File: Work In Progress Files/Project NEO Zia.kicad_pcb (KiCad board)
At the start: 2 copper layers, 220.2 x 220.2 mm, 149 parts, among them J1 TSM-103-02-L-SH-LC, J2 TSM-103-02-L-SH-LC, J3 Conn_01x02, U2 LM1084IS-5.0_NOPB

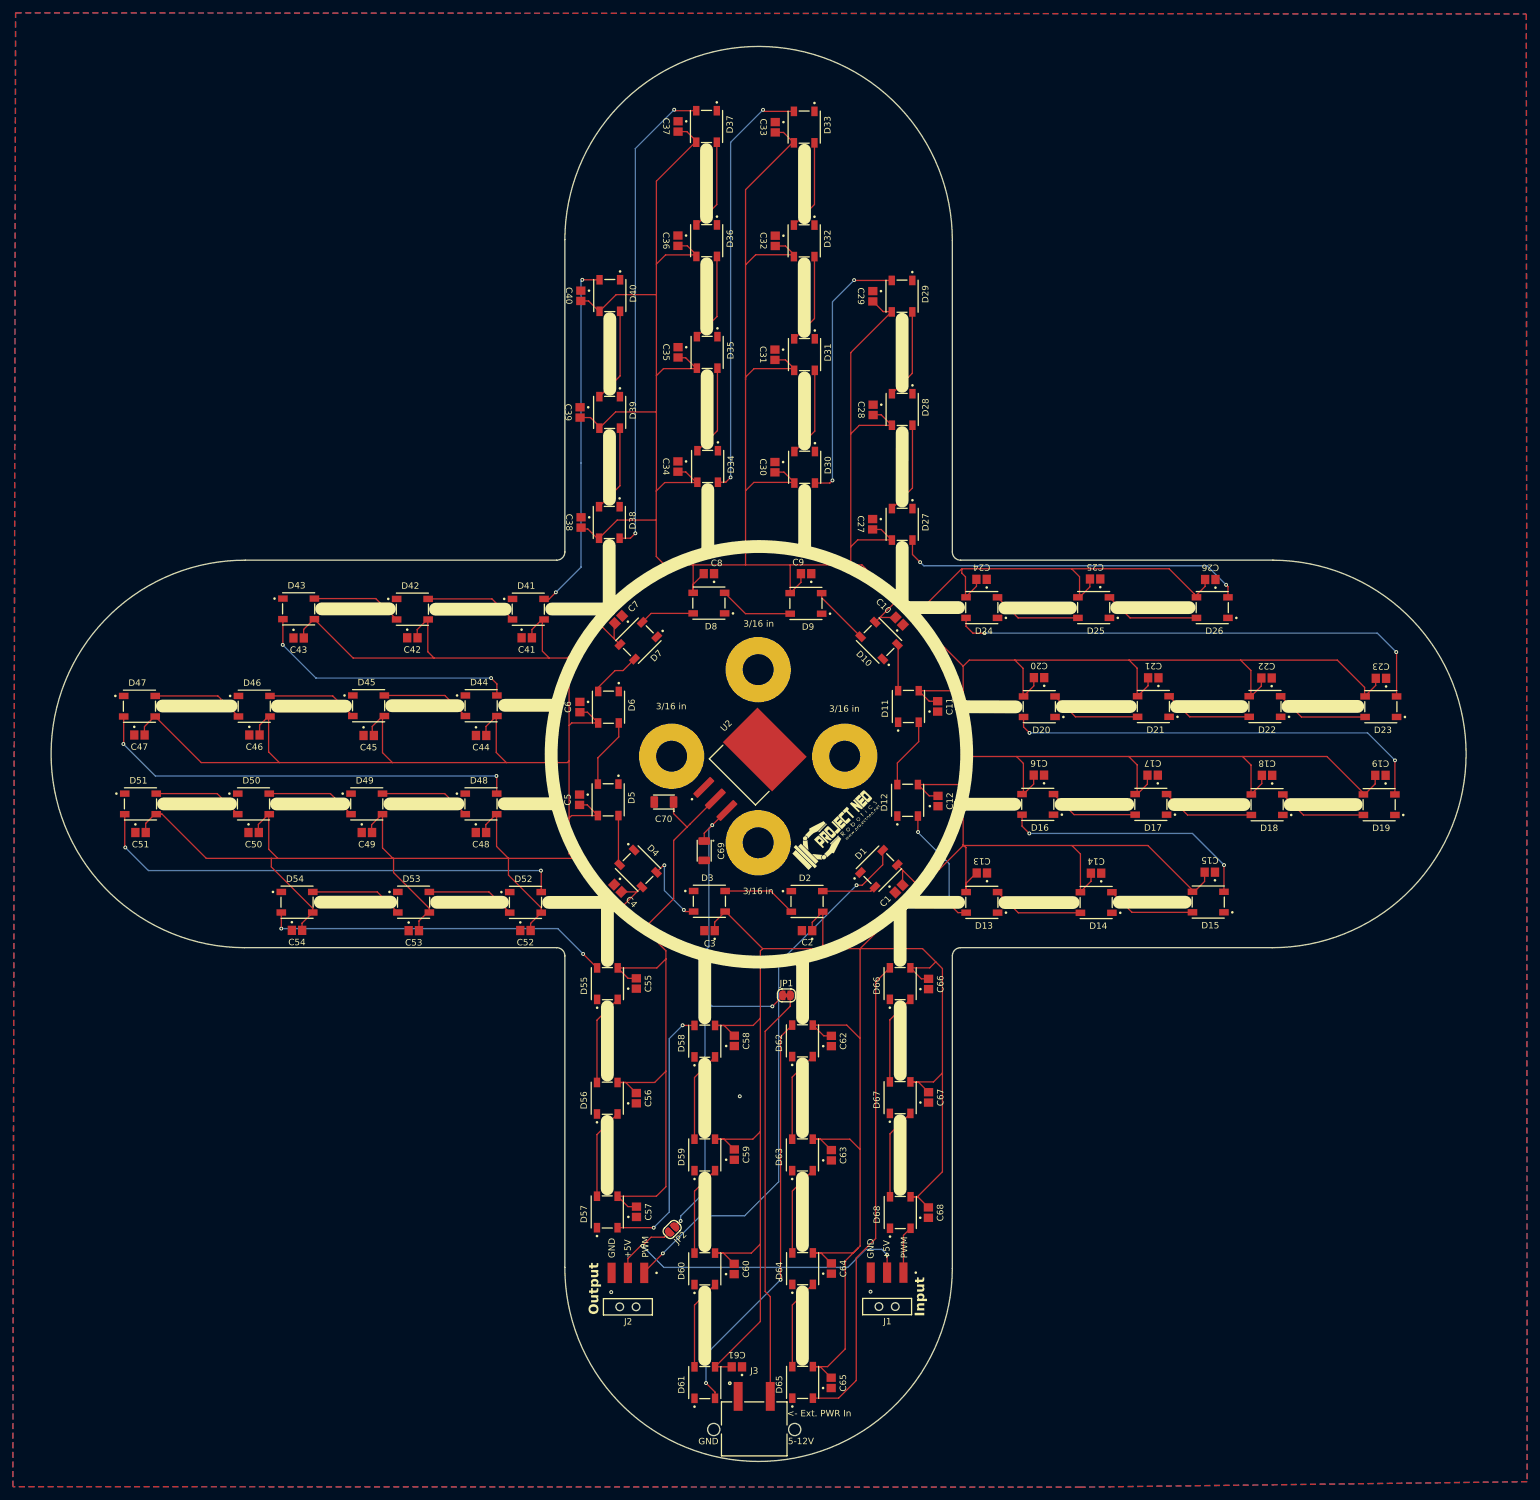
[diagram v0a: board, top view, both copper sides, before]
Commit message: - Added 5V copper plane in center for TI LM1084 voltage regulator - Rearranged filter capacitors for voltage regulator and some NeoPixel's - Added REV marker to board 	# On Rear Silkscreen - Added Jumper Config. Table 	# On Rear Silkscreen - Moved Designer name to rear silkscreen
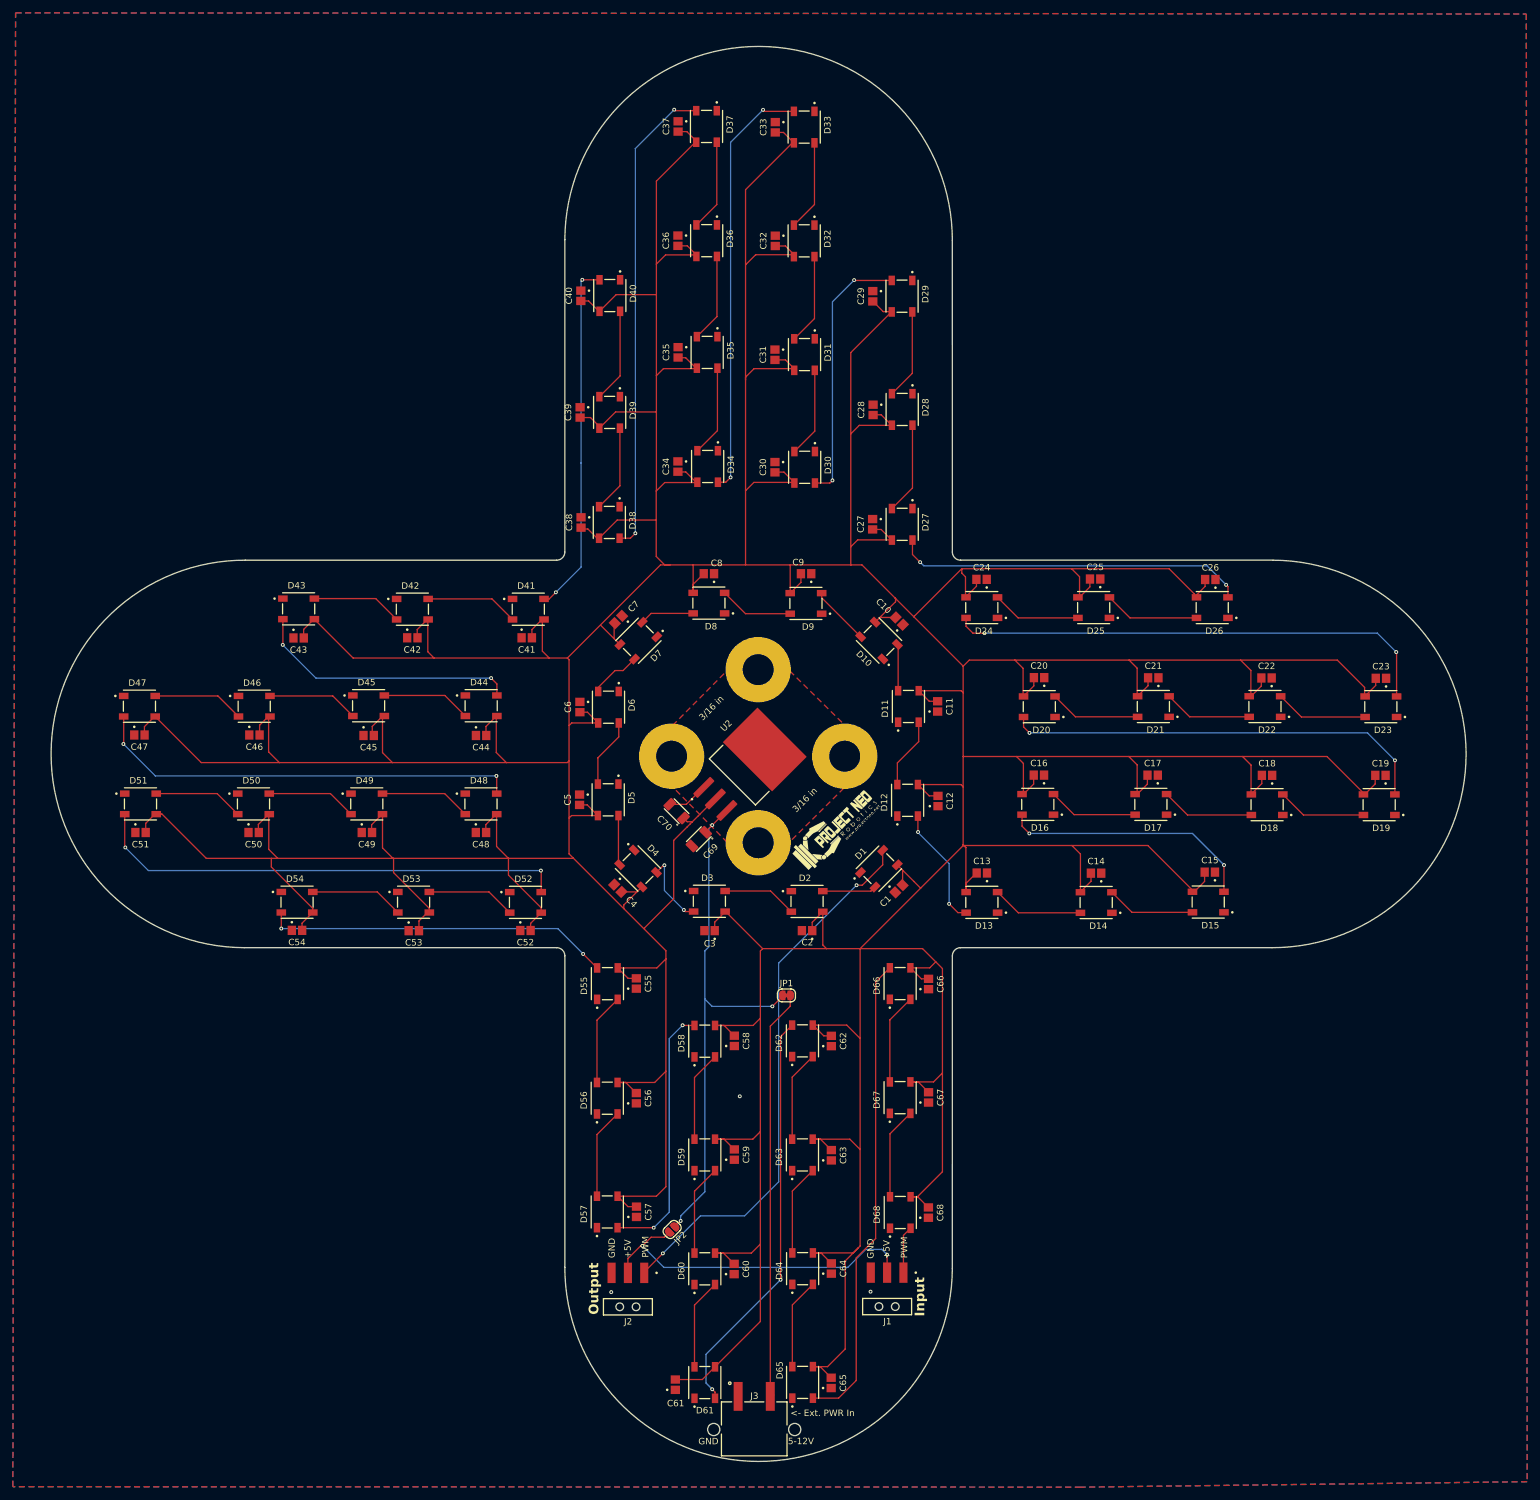
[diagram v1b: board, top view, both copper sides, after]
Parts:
- moved C61 9.97 mm to (173.2, 238.9), turned to -90 degrees
- moved C70 2.44 mm to (173.3, 149.7), turned to 135 degrees
- moved C69 1.99 mm to (176.8, 154.0), turned to -135 degrees
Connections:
- U2 pad 4: GND -> +5V
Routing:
- net GND: track 0.00 -> 6.38 mm
- net Net-(JP1-A): track 84.8 -> 83.1 mm
- net +5V: track 1652.9 -> 1654.1 mm
- added copper zone on F.Cu, net +5V
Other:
- board text added: "Information about this board is avalible at: https://github.com/JZRod/Project-NEO-Zia"
- board text added: "JP1 is bridged by default"
- board text added: "REV 8"
